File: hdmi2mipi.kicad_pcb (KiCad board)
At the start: 4 copper layers, 55 x 55 mm, 100 parts, among them J1 IO, J2 HDMI_A_1.4, J4 Conn_01x04, J5 Conn_01x04, J6 Conn_01x03, J8 AudioJack3, J9 QWIIC, Q1 BC846, Q2 BC846, Q3 BC846, Q4 BC846, Q5 BC846, Q6 BC846, Q7 2SC2712, U10 SY8079AAC, U11 SY8079AAC, U8 MS4344, U9 SY8079AAC, X1 SG-210STF

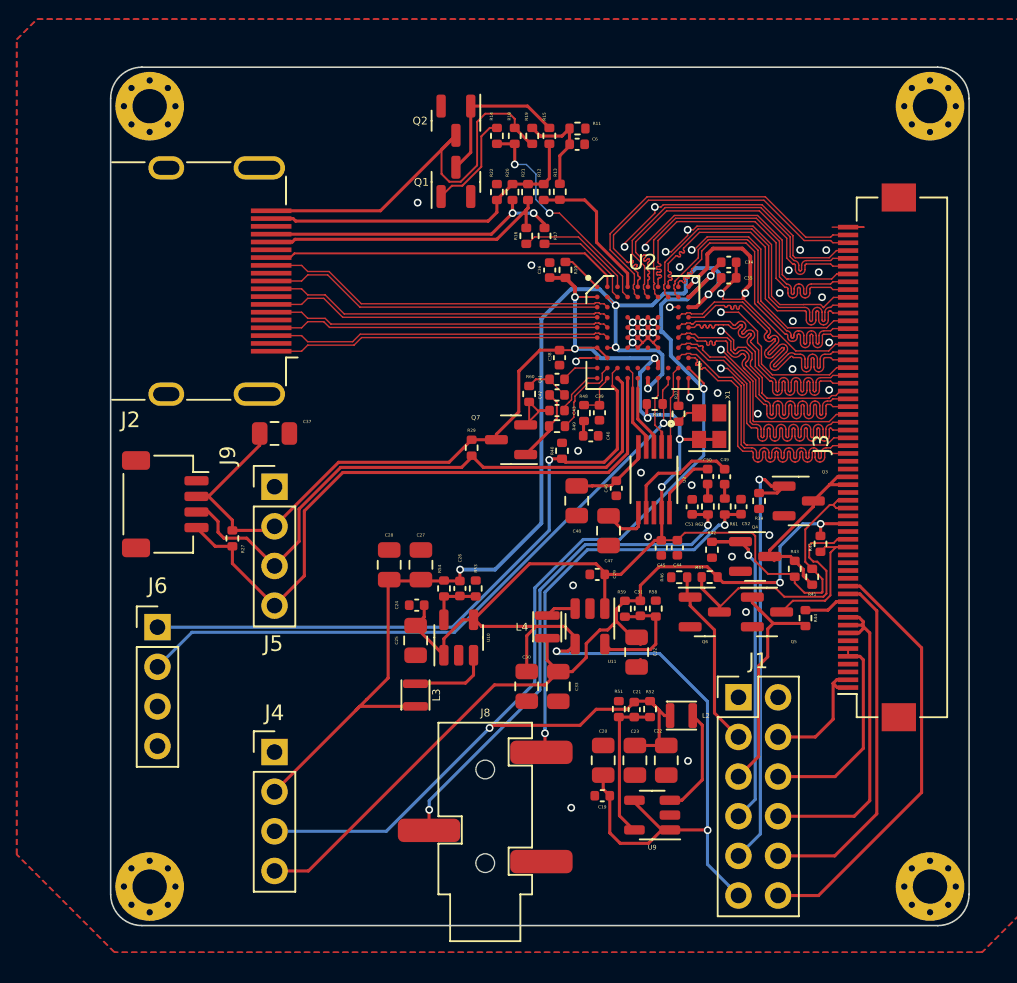
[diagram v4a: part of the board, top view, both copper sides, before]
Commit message: changed layout
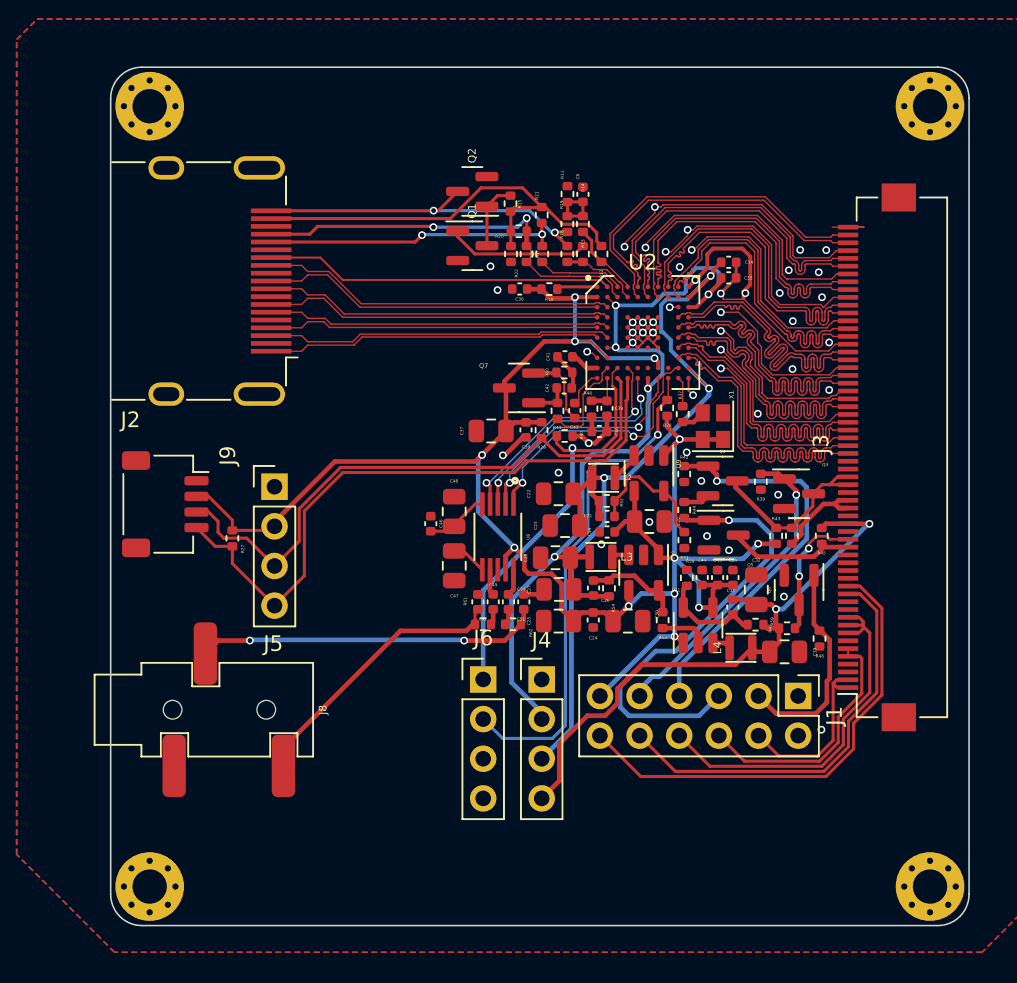
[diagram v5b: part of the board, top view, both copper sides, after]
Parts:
- moved U9 21.9 mm to (6.99, -1.48), turned to -90 degrees
- moved J6 21.1 mm to (-3.63, 11.7)
- moved J8 19.7 mm to (-21.5, 13.7), turned to -90 degrees
- moved C22 18.4 mm to (1.19, -0.17), turned to 180 degrees
- moved C52 17.9 mm to (-3.97, 6.76)
- moved J4 17.7 mm to (0.12, 11.7)
- moved R61 17.2 mm to (-3.64, 8.20), turned to 180 degrees
- moved C19 16.9 mm to (4.31, 2.28)
- moved C49 16.9 mm to (-2.99, 6.76)
- moved L2 16.0 mm to (4.08, -1.19)
- moved C23 15.7 mm to (1.61, 1.87), turned to 180 degrees
- moved C20 15.6 mm to (7.02, 1.61), turned to 0 degrees
- moved C50 15.1 mm to (-2.01, 6.76)
- moved L3 14.8 mm to (3.92, 3.88), turned to 0 degrees
- moved C33 14.7 mm to (15.7, 9.96), turned to 0 degrees
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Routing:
- net 3V3_HDMI: track 169.1 -> 130.7 mm, vias 8 -> 12
- net +1V2: track 78.6 -> 51.9 mm
- net +1V1: track 74.9 -> 58.7 mm
- net Net-(J6-Pin_1): track 42.5 -> 26.8 mm
- net +1V8: track 54.7 -> 39.3 mm
- net 1V8_S2: track 15.1 -> 29.1 mm, vias 0 -> 1
- net Net-(U2-A_SD0): track 5.29 -> 17.1 mm, vias 0 -> 2
- net Net-(U2-A_SCK): track 4.67 -> 15.4 mm, vias 0 -> 2
- net /AUDIO_R: track 32.7 -> 22.1 mm
- net Net-(U2-A_OSCK): track 5.55 -> 16.0 mm, vias 0 -> 2
- net Net-(U2-A_WFS): track 4.84 -> 15.2 mm, vias 0 -> 2
- net Net-(U2-HPDO): track 14.8 -> 4.90 mm, vias 2 -> 0
- net Net-(J6-Pin_2): track 42.1 -> 32.4 mm
- net /AUDIO_L: track 25.7 -> 16.9 mm, vias 2 -> 0
- net Net-(J3-1.8-S1): track 17.0 -> 8.61 mm, vias 0 -> 2
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
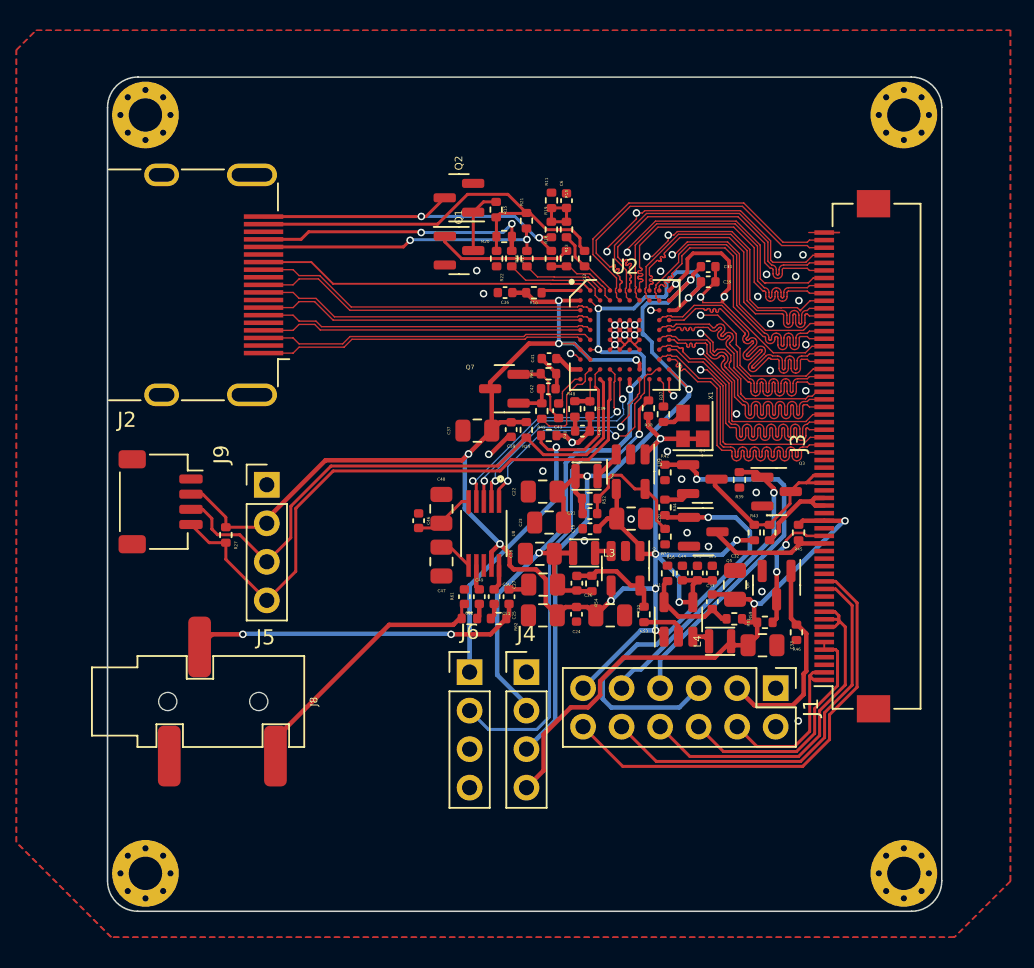
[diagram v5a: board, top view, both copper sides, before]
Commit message: made smaller board
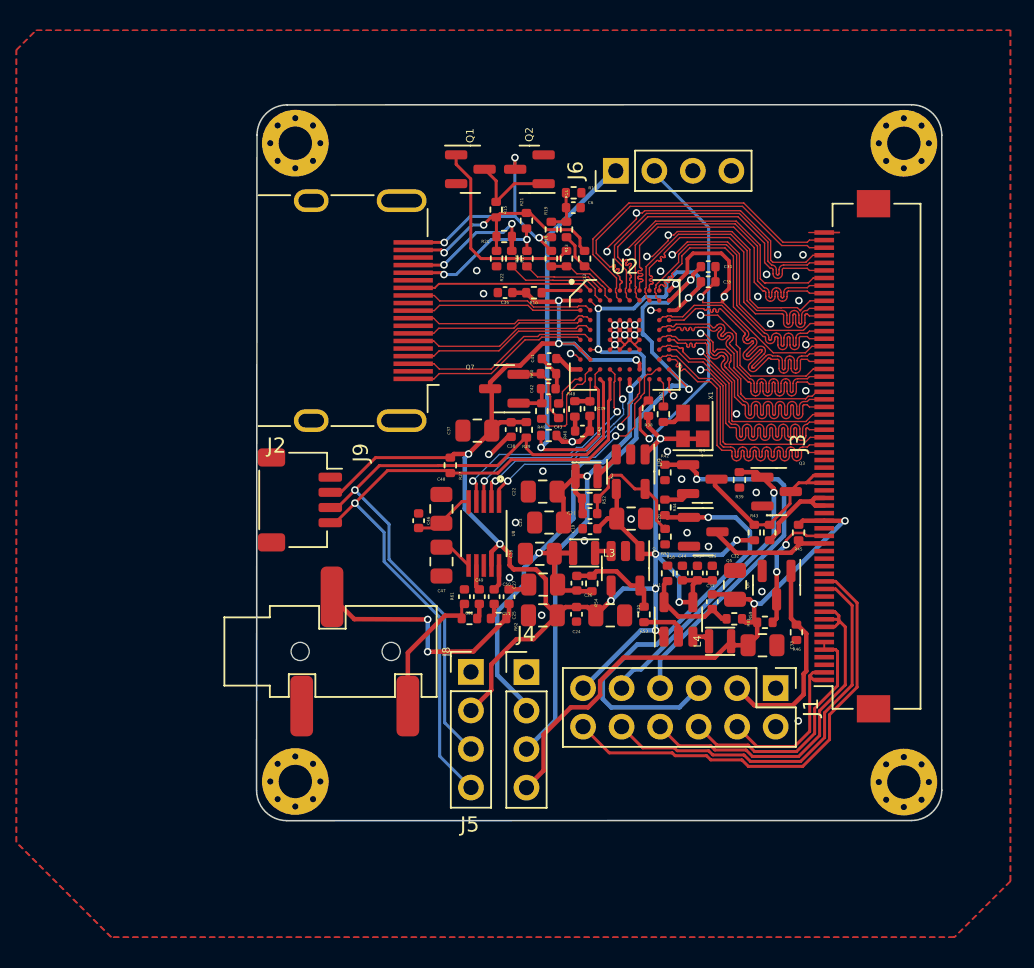
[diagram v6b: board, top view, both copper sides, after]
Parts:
- moved J6 34.4 mm to (6.01, -21.3), turned to 90 degrees
- moved J5 18.3 mm to (-3.54, 11.7)
- moved R27 15.5 mm to (-4.90, -1.90)
- moved H4 11.6 mm to (-15.1, 18.9)
- moved H1 10.1 mm to (-15.1, -23.1)
- moved J2 10.0 mm to (-10.6, -12.1)
- moved J8 9.33 mm to (-12.8, 10.4)
- moved J9 9.19 mm to (-14.8, 0.38)
- moved H3 6.02 mm to (25.0, 19.0)
- moved Q1 5.41 mm to (-3.58, -21.4)
- moved Q2 5.01 mm to (0.31, -21.4)
- moved H2 1.87 mm to (25.0, -23.1)
- moved R11 1.54 mm to (3.23, -19.9), turned to 180 degrees
- moved C6 0.64 mm to (3.21, -18.9), turned to 0 degrees
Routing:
- net Net-(J2-+5V): track 28.2 -> 16.2 mm, vias 0 -> 2
- net /HDMI_C_P: track 21.9 -> 11.3 mm
- net /HDMI_C_N: track 22.7 -> 12.1 mm
- net Net-(J2-CEC): track 22.3 -> 12.0 mm
- net /HDMI_0_N: track 22.4 -> 12.2 mm
- net /HDMI_0_P: track 21.6 -> 11.4 mm
- net /HDMI_1_N: track 22.0 -> 12.5 mm
- net /HDMI_1_P: track 21.2 -> 11.7 mm
- net Net-(J2-SDA): track 18.6 -> 9.41 mm
- net /HDMI_2_N: track 22.1 -> 12.9 mm
- net /HDMI_2_P: track 21.4 -> 12.2 mm
- net Net-(J2-SCL): track 19.2 -> 10.0 mm
- net /AUDIO_L: track 16.9 -> 9.17 mm
- net Net-(J6-Pin_2): track 32.4 -> 25.3 mm
- net Net-(J5-Pin_3): track 38.5 -> 45.4 mm, vias 0 -> 1
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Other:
- board size 55 x 55 mm -> 45.2 x 47.2 mm

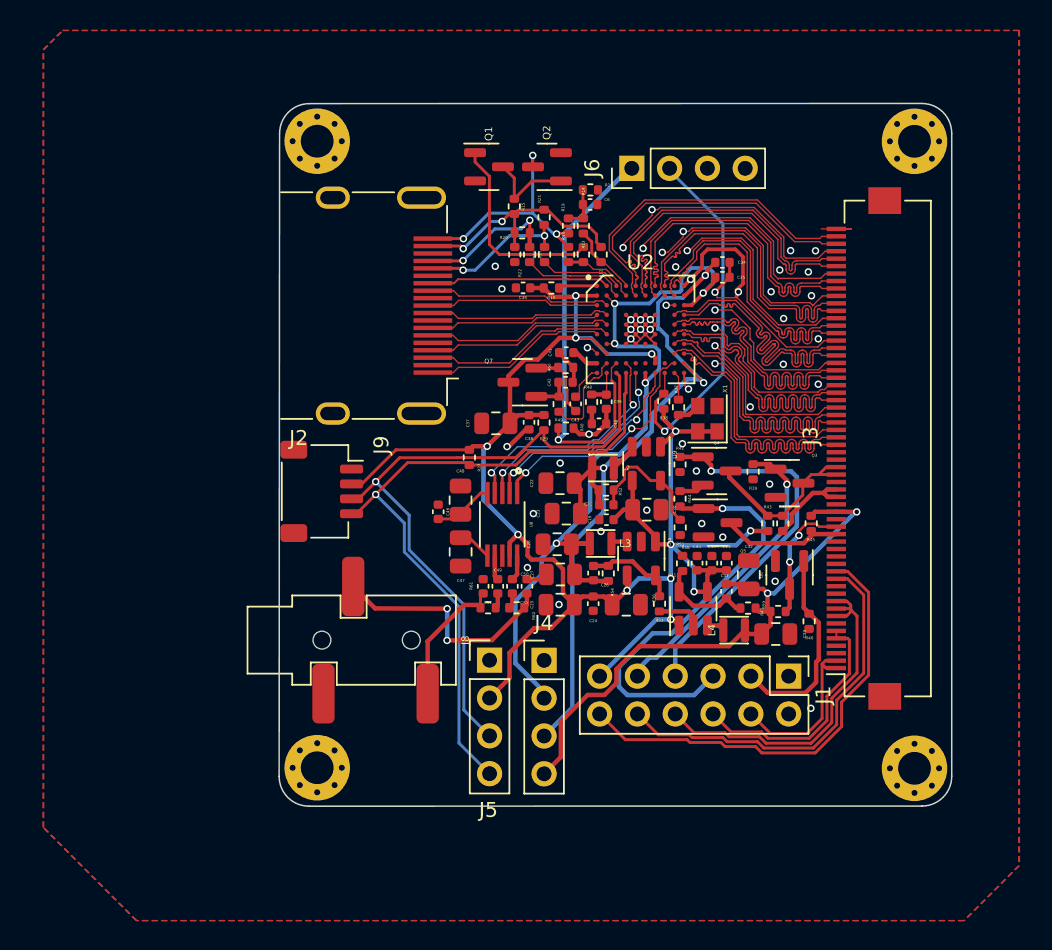
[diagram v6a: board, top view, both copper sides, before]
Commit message: Small fixes and combine 2.54mm headers
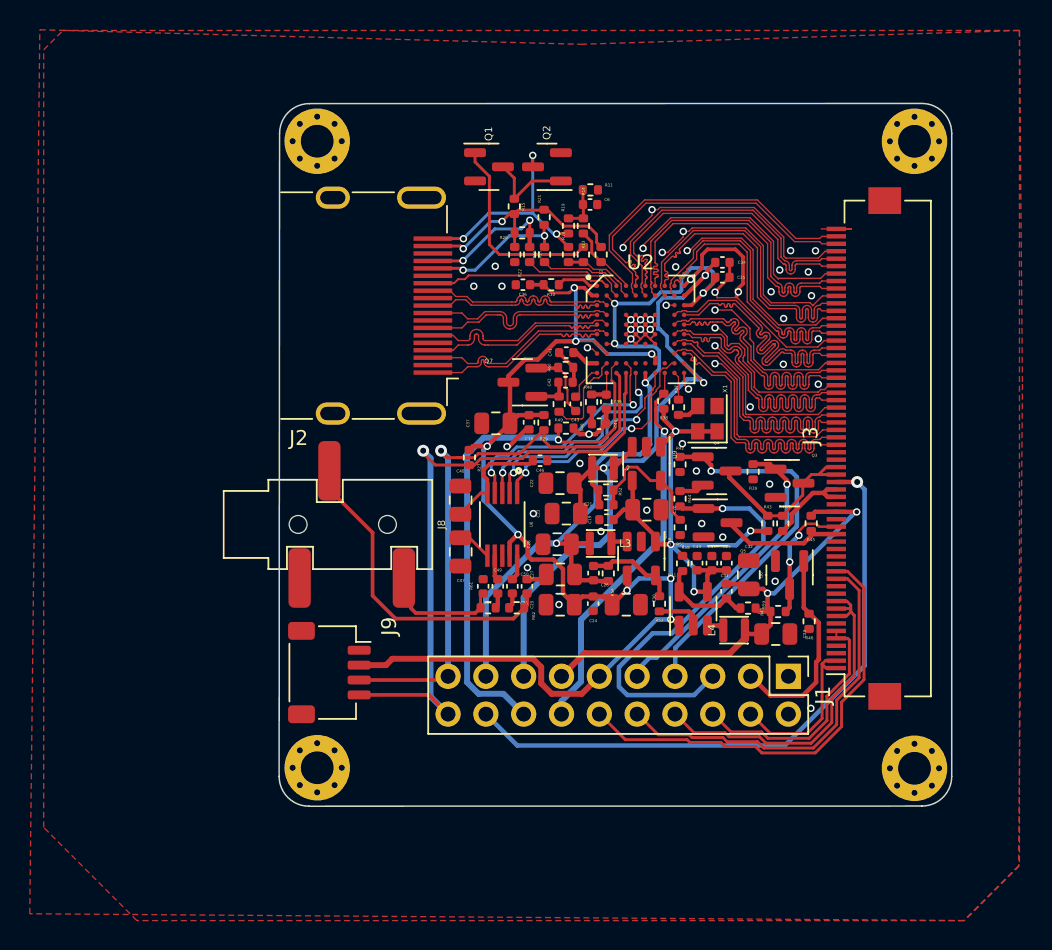
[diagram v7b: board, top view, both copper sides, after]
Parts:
- removed J4, J5: Conn_01x04, Connector_PinHeader_2.54mm:PinHeader_1x04_P2.54mm_Vertical
- removed J6: Conn_01x03, Connector_PinHeader_2.54mm:PinHeader_1x04_P2.54mm_Vertical
- J1: footprint Connector_PinHeader_2.54mm:PinHeader_2x06_P2.54mm_Vertical -> Connector_PinHeader_2.54mm:PinHeader_2x10_P2.54mm_Vertical
- moved J9 12.2 mm to (-14.3, 12.6)
- moved J8 7.93 mm to (-14.4, 2.60)
- moved C46 7.65 mm to (-0.15, -1.68), turned to 0 degrees
- moved R10 0.22 mm to (0.60, -13.5)
- moved C36 0.21 mm to (-1.30, -13.5)
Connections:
- J9 pad 3: Net-(J5-Pin_3) -> SDA
- J9 pad 4: Net-(J5-Pin_4) -> SCL
- R27 pad 2: Net-(J5-Pin_4) -> SCL
- R29 pad 2: Net-(J5-Pin_3) -> SDA
- R38 pad 2: Net-(J6-Pin_2) -> RESET
- R40 pad 1: Net-(J6-Pin_1) -> INT
- U2 pad J3: Net-(J6-Pin_1) -> INT
- U2 pad K3: Net-(J5-Pin_3) -> SDA
- U2 pad K4: Net-(J5-Pin_4) -> SCL
- U2 pad K8: Net-(J6-Pin_2) -> RESET
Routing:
- net Net-(J5-Pin_4): track 46.7 -> 0.00 mm, vias 1 -> 0
- net Net-(J5-Pin_3): track 45.4 -> 0.00 mm, vias 1 -> 0
- net SCL: track 0.00 -> 44.1 mm, vias 0 -> 1
- net VIN: track 0.00 -> 42.6 mm, vias 0 -> 1
- net SDA: track 0.00 -> 40.3 mm, vias 0 -> 1
- net INT: track 0.00 -> 36.3 mm, vias 0 -> 1
- net Net-(J6-Pin_1): track 30.0 -> 0.00 mm, vias 1 -> 0
- net RESET: track 0.00 -> 26.2 mm, vias 0 -> 1
- net Net-(J6-Pin_2): track 25.3 -> 0.00 mm, vias 1 -> 0
- net /AUDIO_R: track 16.0 -> 22.7 mm, vias 2 -> 0
- net +1V8: track 39.3 -> 33.3 mm
- net Net-(U8-VQ): track 4.82 -> 7.56 mm
- net /HDMI_2_P: track 12.2 -> 14.6 mm
- net /HDMI_0_P: track 11.4 -> 13.4 mm
- net /HDMI_2_N: track 12.9 -> 14.6 mm
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
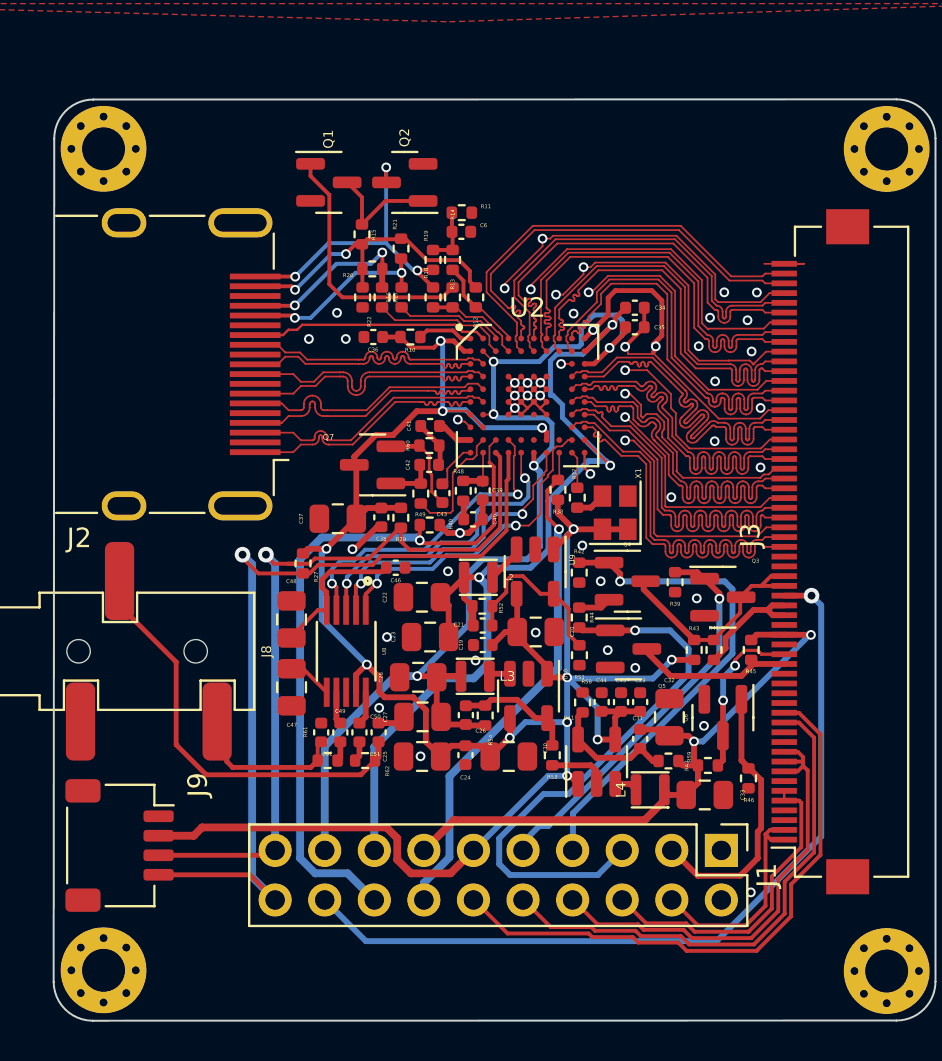
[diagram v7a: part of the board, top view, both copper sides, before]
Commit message: Fixed some routing issues and a bunch of DRC rule violations. Set the board setup to JLCPCB constraints.
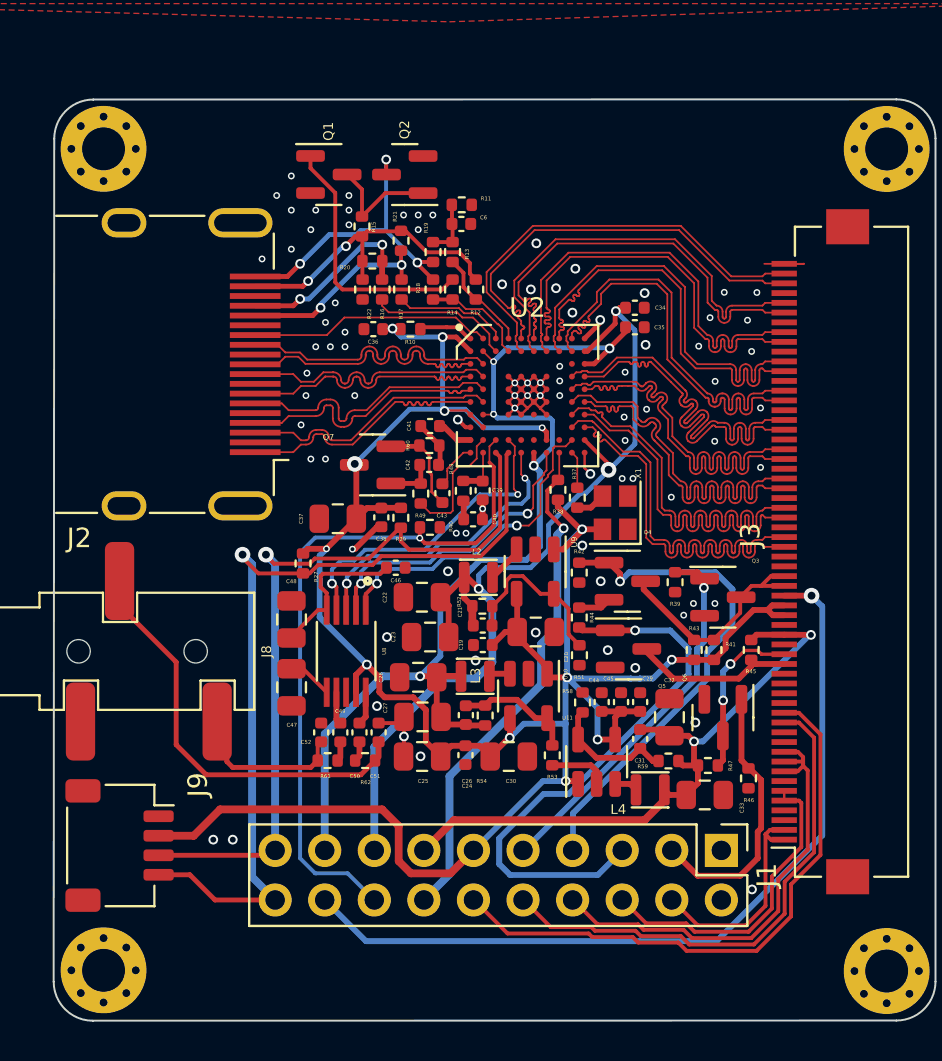
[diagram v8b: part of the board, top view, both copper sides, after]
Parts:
- moved Q1 0.40 mm to (-3.58, -21.8)
- moved R13 0.40 mm to (2.76, -17.9)
- moved R19 0.40 mm to (1.76, -17.9)
- moved R20 0.40 mm to (-1.35, -17.4)
- moved C36 0.40 mm to (-1.30, -13.9)
- moved R10 0.40 mm to (0.60, -13.9)
- moved R12 0.40 mm to (3.95, -15.9)
- moved R14 0.40 mm to (2.76, -15.9)
- moved R16 0.40 mm to (0.15, -15.9)
- moved R17 0.40 mm to (-0.85, -15.9)
- moved R18 0.40 mm to (1.76, -15.9)
- moved R22 0.40 mm to (-1.85, -15.9)
- moved C6 0.40 mm to (3.21, -19.3)
- moved Q2 0.40 mm to (0.31, -21.8)
- moved R11 0.40 mm to (3.23, -20.3)
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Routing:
- net GND: track 167.9 -> 33.2 mm, vias 53 -> 86
- net +1V1: track 57.5 -> 54.3 mm
- net /AUDIO_R: track 22.7 -> 20.2 mm
- net 3V3_HDMI: track 128.3 -> 130.3 mm, vias 12 -> 13
- net +1V2: track 50.9 -> 49.3 mm
- net 3V3_S2: track 20.0 -> 18.8 mm
- net /HDMI_2_P: track 14.6 -> 13.4 mm
- net /HDMI_2_N: track 14.6 -> 13.5 mm
- net /HDMI_C_N: track 12.3 -> 13.4 mm
- net /HDMI_C_P: track 12.3 -> 13.3 mm
- net SDA: track 40.3 -> 39.3 mm
- net /AUDIO_L: track 7.81 -> 7.10 mm
- net Net-(U2-A_WFS): track 15.9 -> 15.2 mm
- net +1V8: track 33.3 -> 32.8 mm
- net /HDMI_1_N: track 13.5 -> 14.0 mm
